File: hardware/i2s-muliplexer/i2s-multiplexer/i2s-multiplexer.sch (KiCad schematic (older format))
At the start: 31 parts, among them J1 Conn_01x05, J2 Conn_01x05, J3 Conn_01x05, J4 Conn_01x05, J5 Conn_01x05, J6 Conn_01x05, J7 Conn_01x07, J8 Conn_01x05, U1 74HC244, U2 74HC244, U3 74HC244, U4 74HC126, U5 74LS138

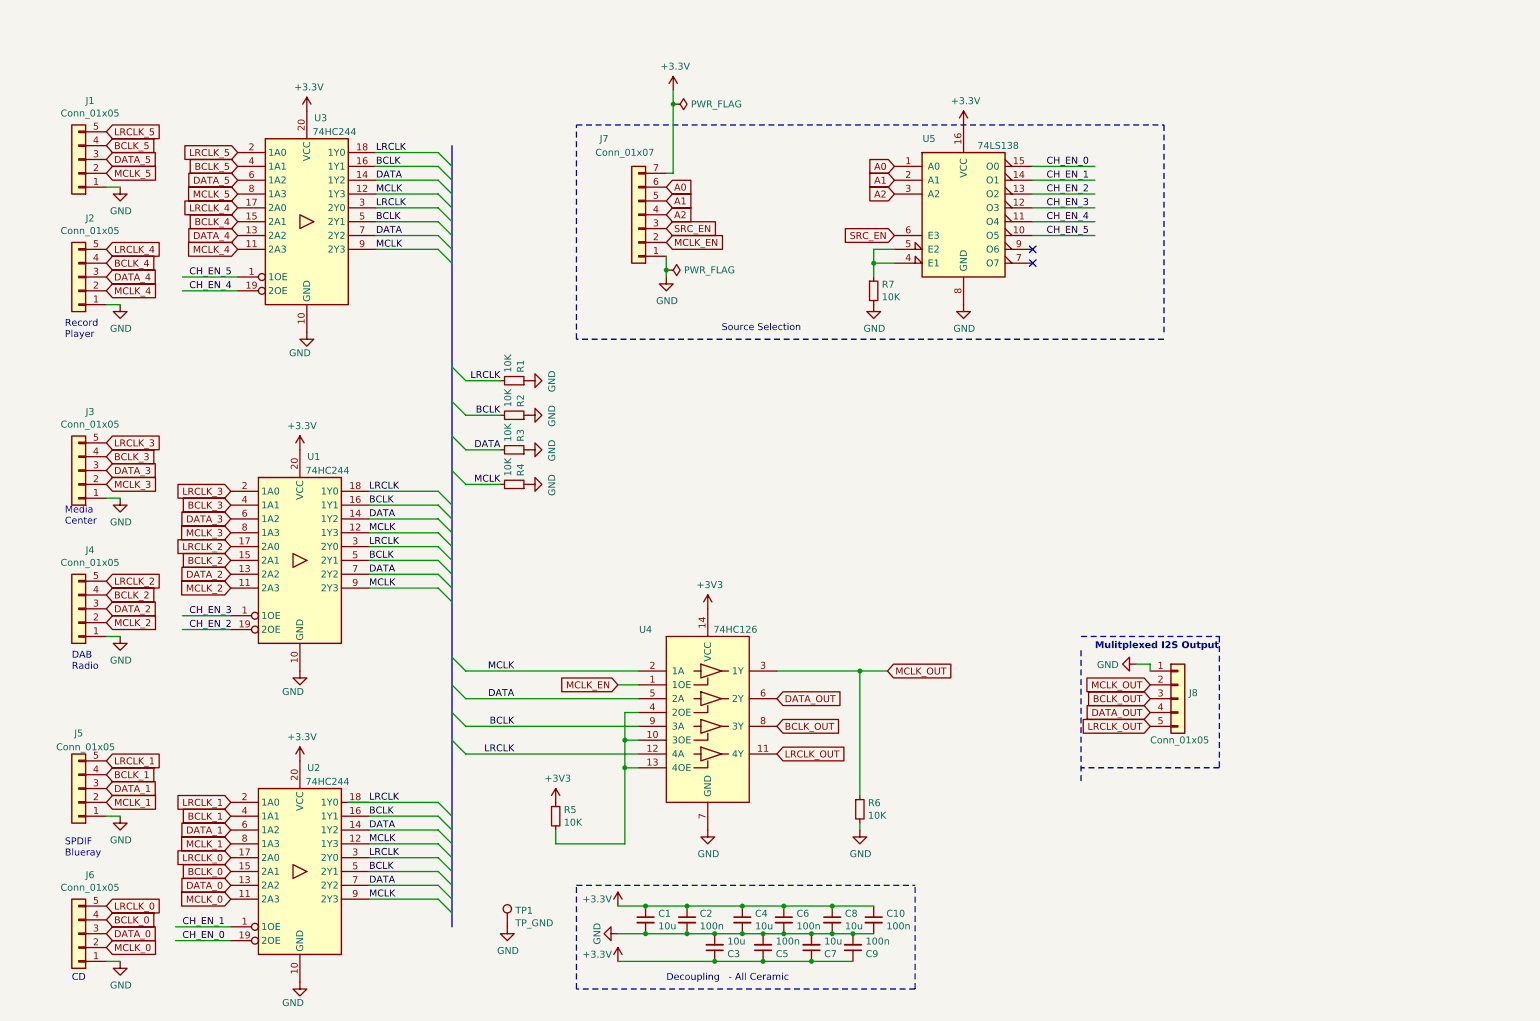
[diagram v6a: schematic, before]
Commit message: Input trace track length tuning
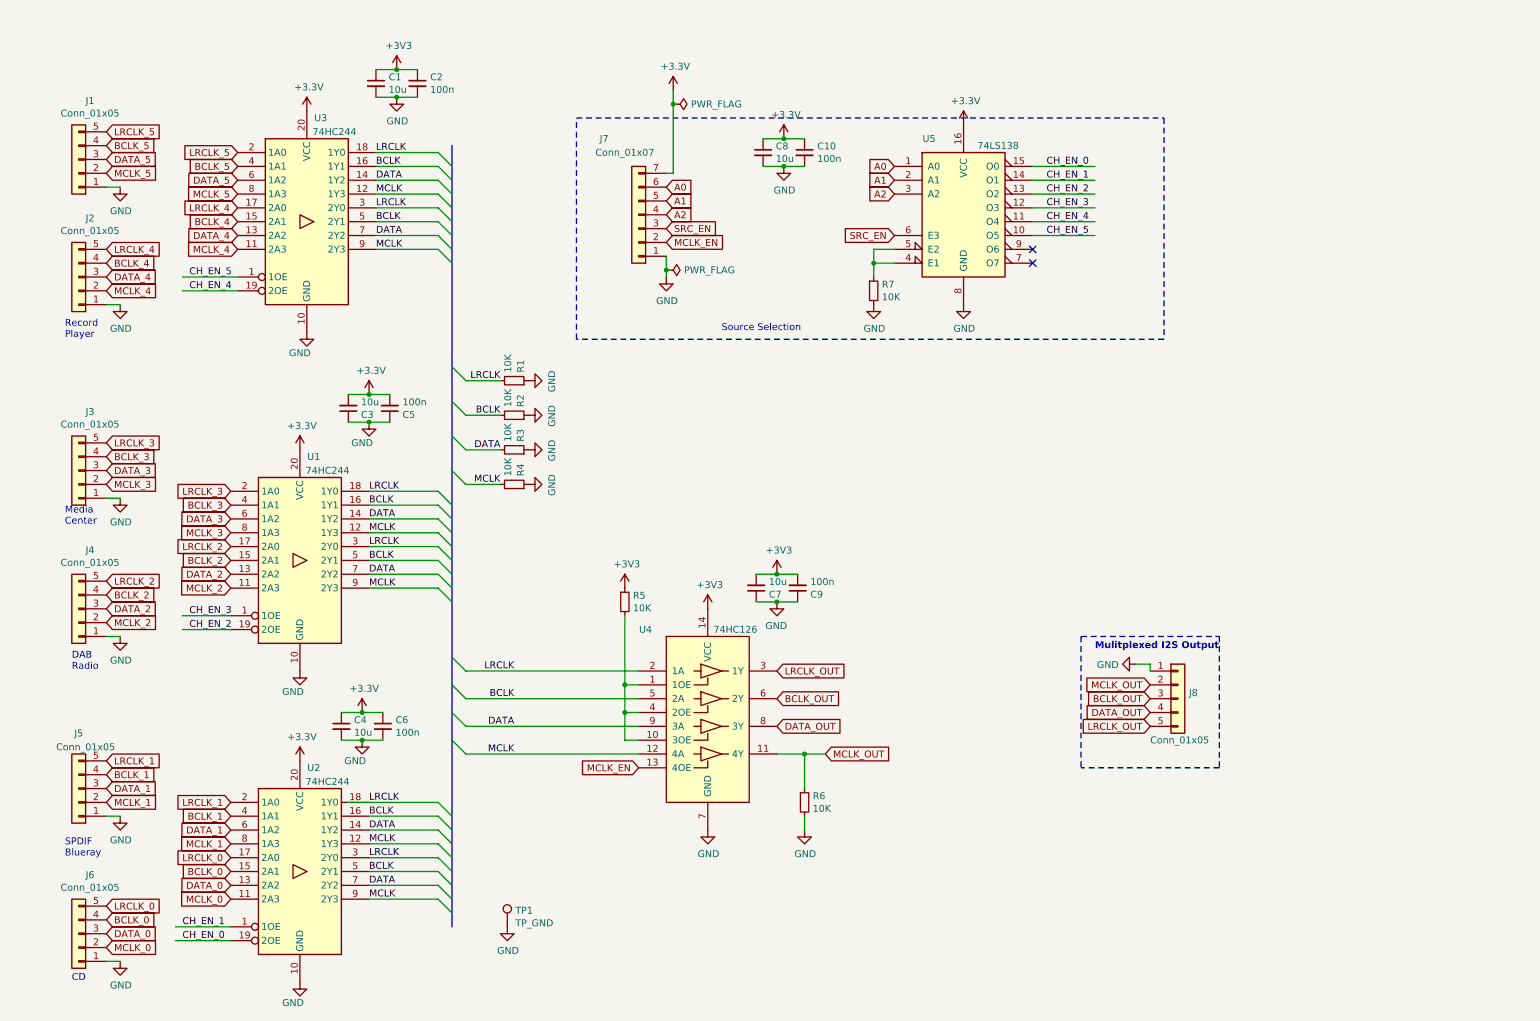
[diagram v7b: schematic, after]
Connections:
- wire segments 94 -> 91
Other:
- note removed: "- All Ceramic"
- note removed: "Decoupling"
- moved on the sheet: C1, C10, C2, C3, C4, C5, C6, C7, C8, C9, R5, R6
